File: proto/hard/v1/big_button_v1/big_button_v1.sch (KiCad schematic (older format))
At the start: 17 parts, among them J1 RJ12, J2 RJ12, J3 Conn_01x02, J4 Conn_01x02, SW1 SW_Push, U1 LM393, U2 PC817, U3 PC817

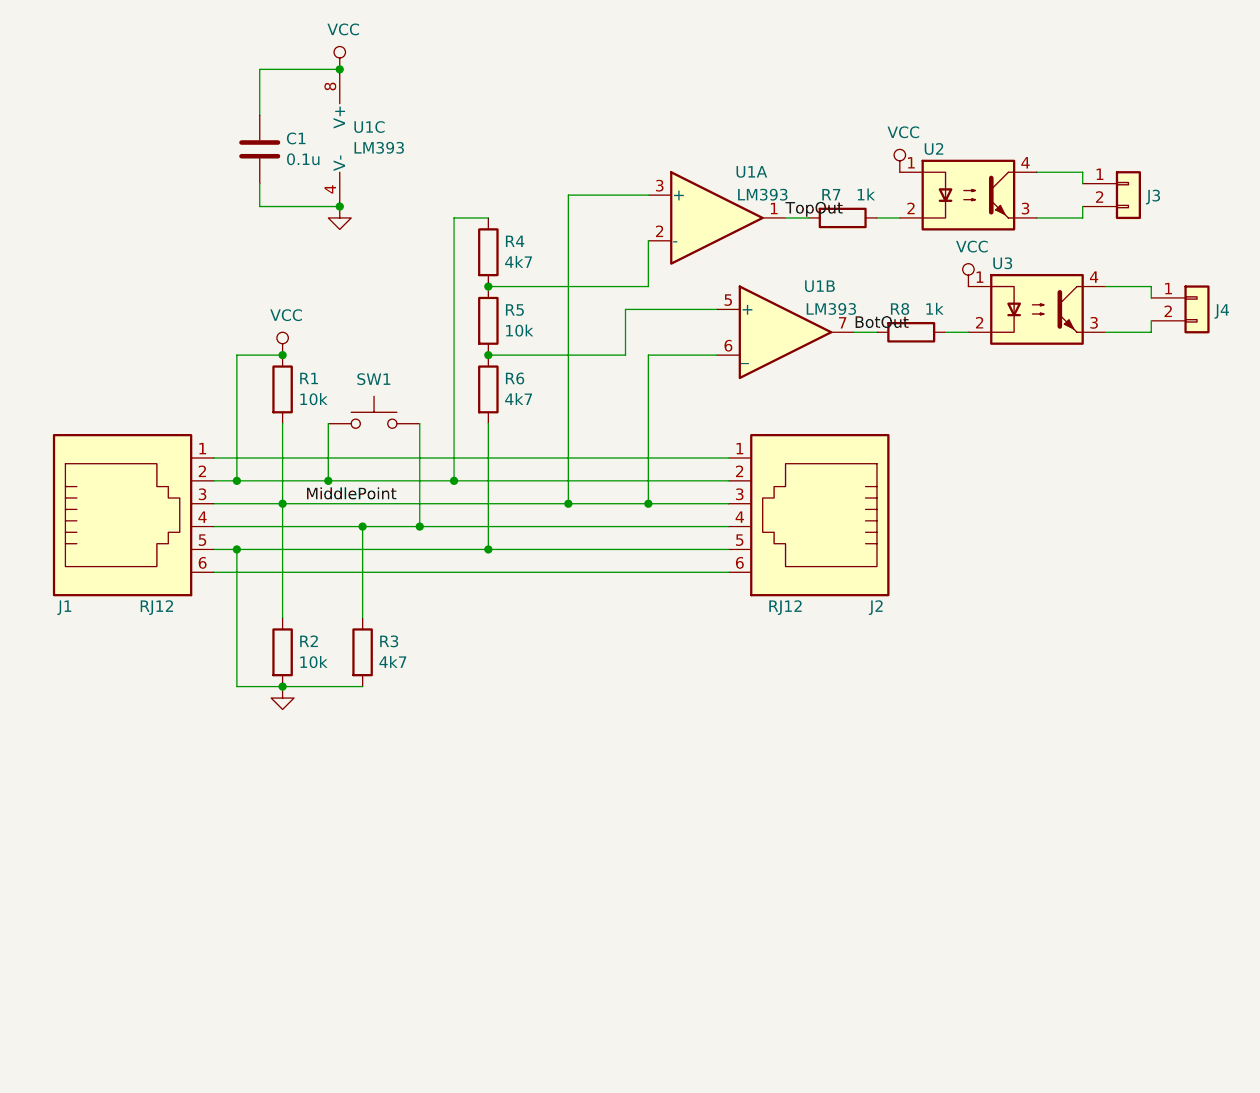
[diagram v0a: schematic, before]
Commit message: Schematic libs clean-up
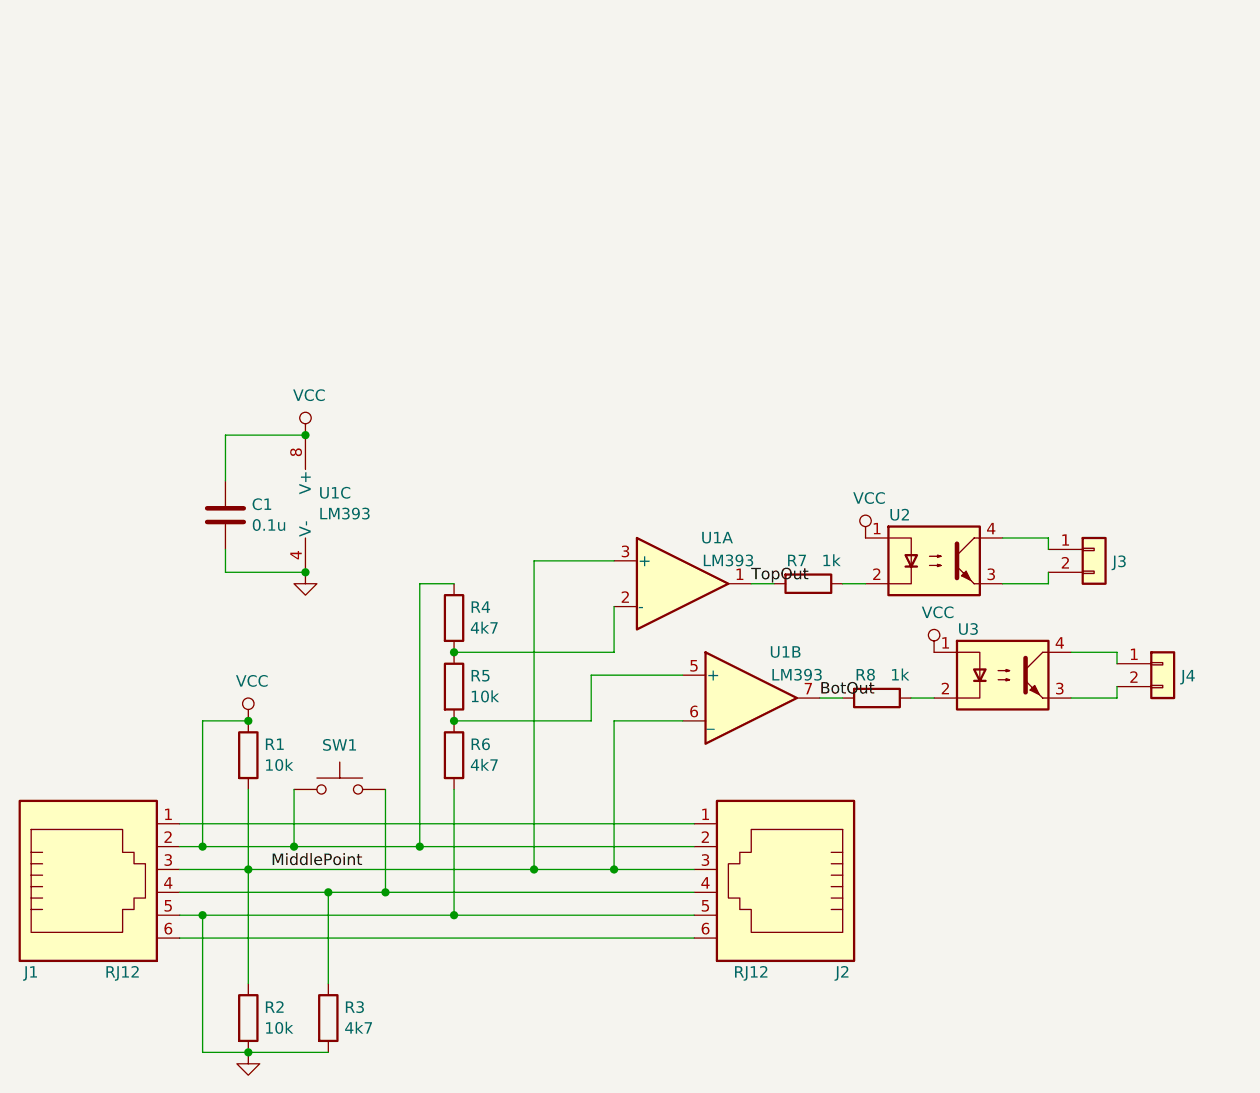
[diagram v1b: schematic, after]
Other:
- moved on the sheet: C1, J1, J2, J3, J4, R1, R2, R3, R4, R5, R6, R7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

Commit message: Button rework - specialization for small case BMW50028. Includes button and single click LED highlight. Added diode to power line. Changed to single comparator.
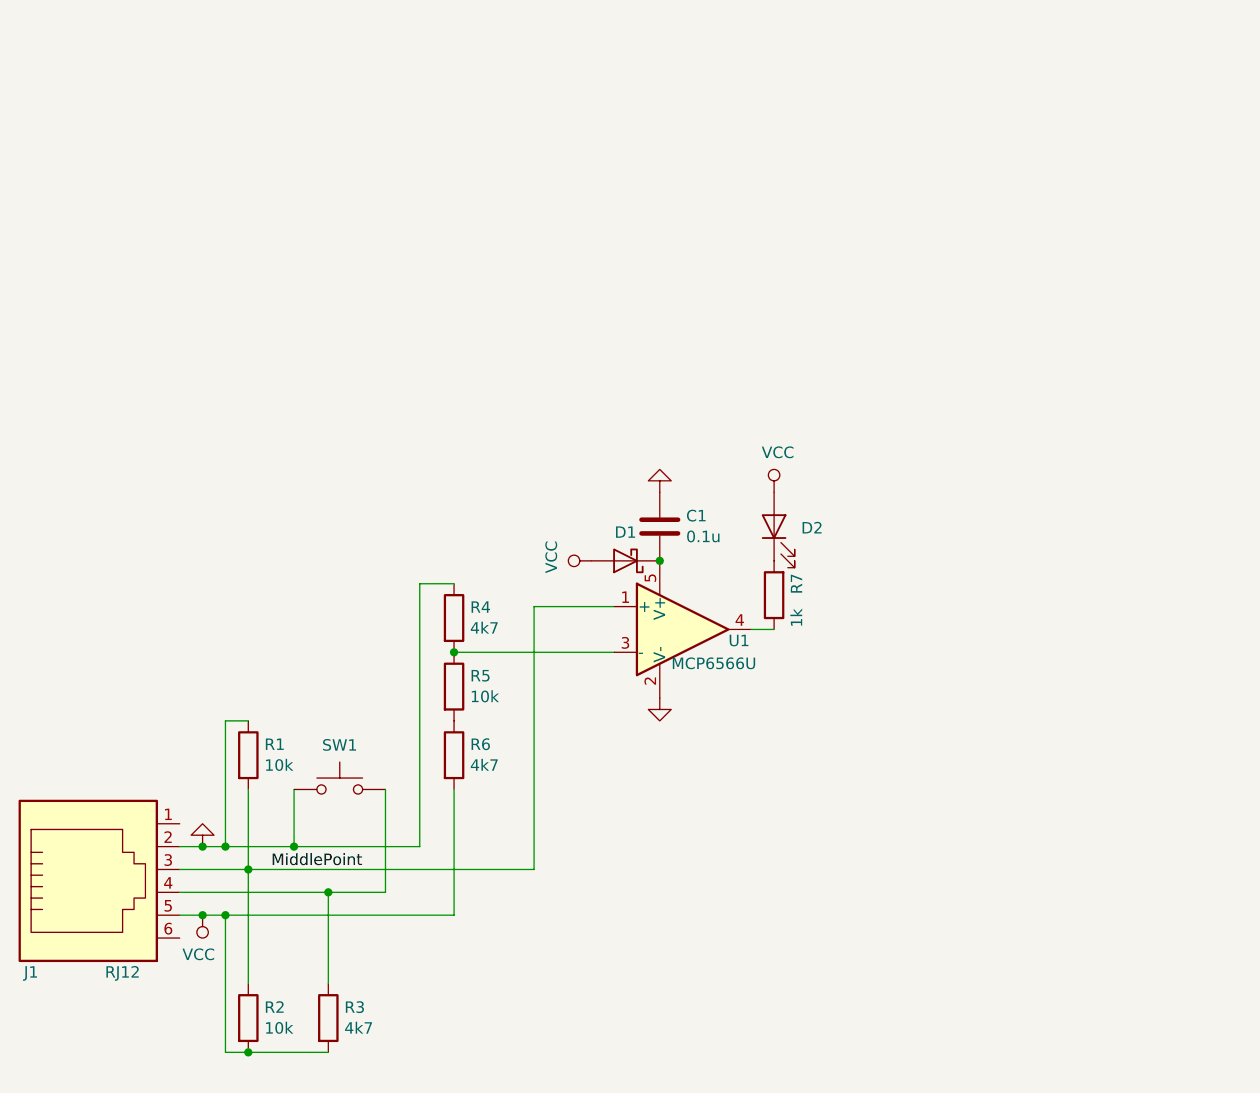
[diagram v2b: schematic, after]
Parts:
- removed J2: RJ12, Connector_RJ:RJ12_Amphenol_54601, symbol Connector:RJ12
- removed J3, J4: Conn_01x02, Connector_JST:JST_EH_B2B-EH-A_1x02_P2.50mm_Vertical, symbol Connector_Generic:Conn_01x02
- removed R8: 1k, Resistor_SMD:R_0805_2012Metric_Pad1.15x1.40mm_HandSolder, symbol Device:R
- removed U1: LM393, Package_SO:SOP-8_3.76x4.96mm_P1.27mm, symbol Comparator:LM393
- removed U2, U3: PC817, Package_DIP:DIP-4_W7.62mm, symbol Isolator:PC817
- added D1: D_Schottky, Diode_SMD:D_SMA-SMB_Universal_Handsoldering, symbol Device:D_Schottky
- added D2: LED, LED_THT:LED_D5.0mm, symbol Device:LED
- added U1: MCP6566U, Package_TO_SOT_SMD:SOT-23-5, symbol Comparator:MCP6566U
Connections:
- net GND: now also C1.1, J1.2, R1.1, R4.1, SW1.1, U1.2 (V-); no longer C1.2, J1.5, R2.2, R3.2, R6.2
- net MiddlePoint: now also U1.1 (+)
- net VCC: now also J1.5, R2.2, R3.2, R6.2, D1.2 (A), D2.2 (A); no longer C1.1, J1.2, R1.1, R4.1, SW1.1
- net at R4.2, R5.1: now also U1.3 (-)
- net at R7.1: now also U1.4
- net TopOut: no longer names the net of R7.2
- net TopOut: now also D2.1 (K)
- new net: C1.2, D1.1 (K), U1.5 (V+)
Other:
- moved on the sheet: C1, R7
